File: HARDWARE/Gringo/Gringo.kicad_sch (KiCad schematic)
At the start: 7 parts, among them J1 Conn_01x06, J3 Conn_01x06, J4 Alim, J5 Conn_01x06, J6 Conn_01x06, J7 Conn_01x06, U2 BQ500212ARGZT

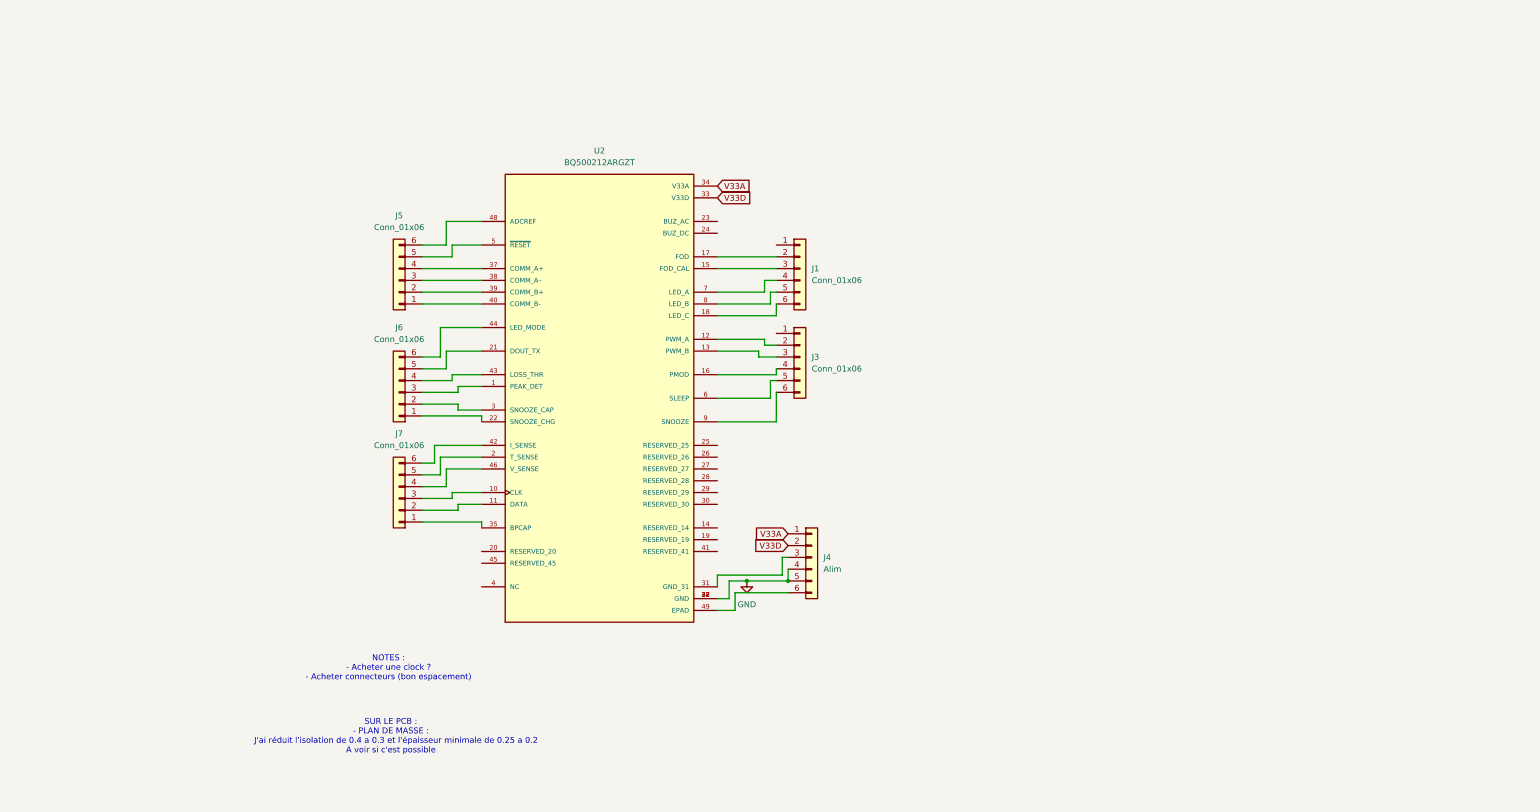
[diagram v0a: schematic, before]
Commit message: PCB test Marius - 3 composants faits
Potentiellement rajouter certains composants avant de le commander (je vais laisser faire MARIUS)
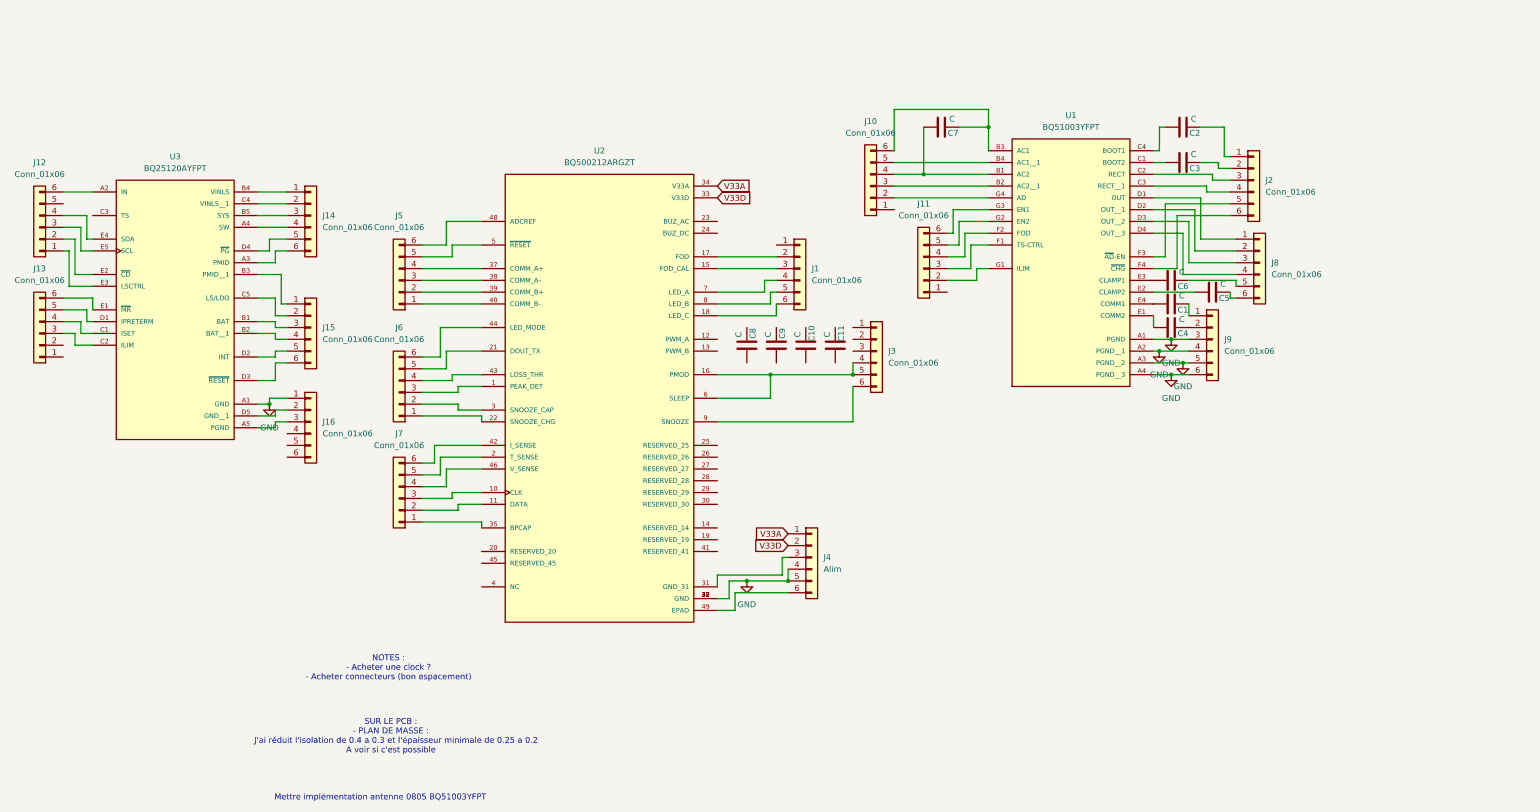
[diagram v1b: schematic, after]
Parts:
- added C1, C10, C11, C2, C3, C4, C5, C6, C7, C8, C9: C, Capacitor_SMD:C_0805_2012Metric, symbol Device:C
- added J10, J11, J12, J13, J14, J15, J16, J2, J8, J9: Conn_01x06, Connector_PinHeader_2.54mm:PinHeader_1x06_P2.54mm_Vertical, symbol Connector_Generic:Conn_01x06
- added U1: BQ51003YFPT, BQ51003YFPT:BGA28N40P7X4_300X188X50N, symbol BQ51003YFPT:BQ51003YFPT
- added U3: BQ25120AYFPT, BQ25120AYFPT:IC_BQ25120AYFPT, symbol BQ25120AYFPT:BQ25120AYFPT
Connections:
- net GND: now also J16.1 (Pin_1), J9.3 (Pin_3), J9.4 (Pin_4), J9.5 (Pin_5), J9.6 (Pin_6), U1.A1 (PGND), U1.A2 (PGND__1), U1.A3 (PGND__2), U1.A4 (PGND__3), U3.A1 (GND)
- net at U2.12 (PWM_A): no longer J3.2 (Pin_2)
- net at U2.13 (PWM_B): no longer J3.3 (Pin_3)
- net at J3.4 (Pin_4), U2.16 (PMOD): now also J3.5 (Pin_5), U2.6 (SLEEP)
- new net: C1.1, U1.E4 (COMM1)
- new net: C1.2, J9.1 (Pin_1)
- new net: J13.3 (Pin_3), U3.C2 (ILIM)
- new net: J13.4 (Pin_4), U3.C1 (ISET)
- new net: J13.5 (Pin_5), U3.D1 (IPRETERM)
- new net: J13.6 (Pin_6), U3.E1 (~{MR})
- new net: J8.1 (Pin_1), U1.D1 (OUT)
- new net: J8.2 (Pin_2), U1.D2 (OUT__1)
- new net: J8.3 (Pin_3), U1.D3 (OUT__2)
- new net: J8.4 (Pin_4), U1.D4 (OUT__3)
- new net: C6.2, J8.5 (Pin_5)
- new net: C5.2, J8.6 (Pin_6)
- new net: C3.1, U1.C1 (BOOT2)
- new net: C3.2, J2.2 (Pin_2)
- new net: C7.1, J10.4 (Pin_4), U1.B1 (AC2)
- new net: C7.2, J10.6 (Pin_6), U1.B3 (AC1)
- new net: J16.2 (Pin_2), U3.D5 (GND__1)
- new net: J16.3 (Pin_3), U3.A5 (PGND)
- new net: J10.3 (Pin_3), U1.B2 (AC2__1)
- new net: J10.5 (Pin_5), U1.B4 (AC1__1)
- new net: J2.3 (Pin_3), U1.C2 (RECT)
- new net: J2.4 (Pin_4), U1.C3 (RECT__1)
- new net: C2.1, U1.C4 (BOOT1)
- new net: C4.1, U1.E1 (COMM2)
- new net: C5.1, U1.E2 (CLAMP2)
- new net: C6.1, U1.E3 (CLAMP1)
- new net: J11.3 (Pin_3), U1.F1 (TS-CTRL)
- new net: J11.4 (Pin_4), U1.F2 (FOD)
- new net: J2.5 (Pin_5), U1.F3 (~{AD}-EN)
- new net: J2.6 (Pin_6), U1.F4 (~{CHG})
- new net: J11.2 (Pin_2), U1.G1 (ILIM)
- new net: J11.5 (Pin_5), U1.G2 (EN2)
- new net: J11.6 (Pin_6), U1.G3 (EN1)
- new net: J10.2 (Pin_2), U1.G4 (AD)
- new net: J15.1 (Pin_1), U3.B3 (PMID__1)
- new net: J15.2 (Pin_2), U3.C5 (LS/LDO)
- new net: J15.3 (Pin_3), U3.B1 (BAT)
- new net: J15.4 (Pin_4), U3.B2 (BAT__1)
- new net: J15.5 (Pin_5), U3.D2 (INT)
- new net: J15.6 (Pin_6), U3.D3 (~{RESET})
- new net: C4.2, J9.2 (Pin_2)
- new net: C2.2, J2.1 (Pin_1)
- new net: J12.1 (Pin_1), U3.E3 (LSCTRL)
- new net: J12.2 (Pin_2), U3.E2 (~{CD})
- new net: J12.3 (Pin_3), U3.E5 (SCL)
- new net: J12.4 (Pin_4), U3.E4 (SDA)
- new net: J12.6 (Pin_6), U3.A2 (IN)
- new net: J14.1 (Pin_1), U3.B4 (VINLS)
- new net: J14.2 (Pin_2), U3.C4 (VINLS__1)
- new net: J14.3 (Pin_3), U3.B5 (SYS)
- new net: J14.4 (Pin_4), U3.A4 (SW)
- new net: J14.5 (Pin_5), U3.D4 (~{PG})
- new net: J14.6 (Pin_6), U3.A3 (PMID)
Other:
- note added: "Mettre implémentation antenne 0805 BQ51003YFPT"
- moved on the sheet: J3

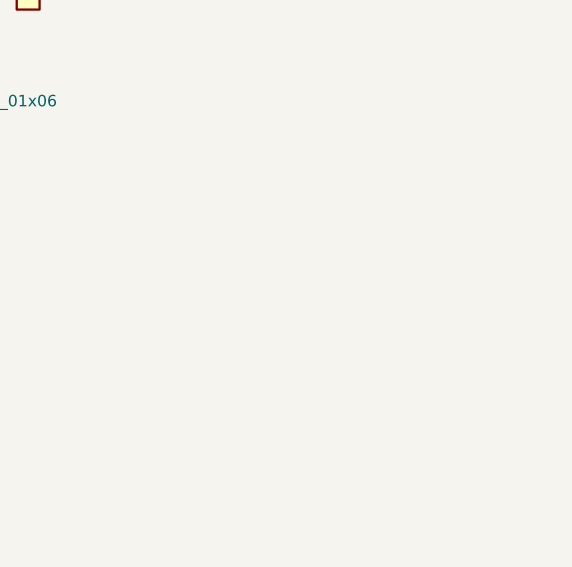
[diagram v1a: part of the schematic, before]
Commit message: Update the eval kit PCB with BPM module part
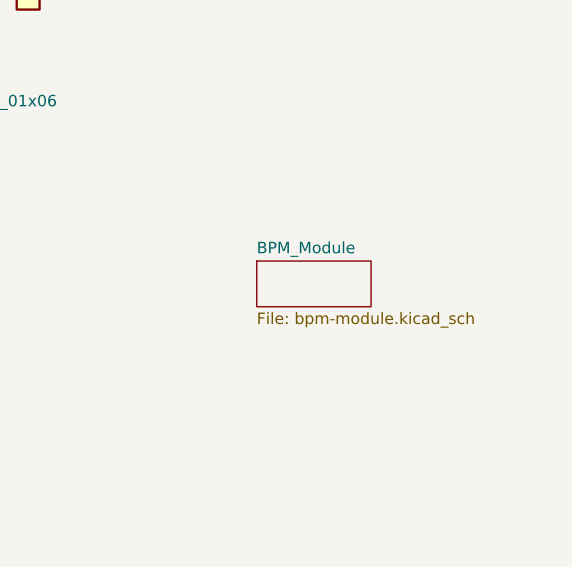
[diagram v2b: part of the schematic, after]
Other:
- added sheet BPM_Module (bpm-module.kicad_sch)
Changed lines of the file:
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@@
+		)
+	)
+	(sheet
+		(at 304.8 110.49)
+		(size 12.7 5.08)
+		(exclude_from_sim no)
+		(in_bom yes)
+		(on_board yes)
+		(dnp no)
+		(fields_autoplaced yes)
+		(stroke
+			(width 0.1524)
+			(type solid)
+		)
+		(fill
+			(color 0 0 0 0.0000)
+		)
+		(property "Sheetname" "BPM_Module"
+			(at 304.8 109.7784 0)
+			(effects
+				(font
+					(size 1.27 1.27)
+				)
+				(justify left bottom)
+			)
+		)
+		(property "Sheetfile" "bpm-module.kicad_sch"
+			(at 304.8 116.1546 0)
+			(effects
+				(font
+					(size 1.27 1.27)
+				)
+				(justify left top)
+			)
+		)
+		(instances
+			(project "Gringo"
+				(path "/d29665dc-a603-413d-b9b9-433aa1d50e1d"
+					(page "2")
+				)
+			)
 		)
 	)

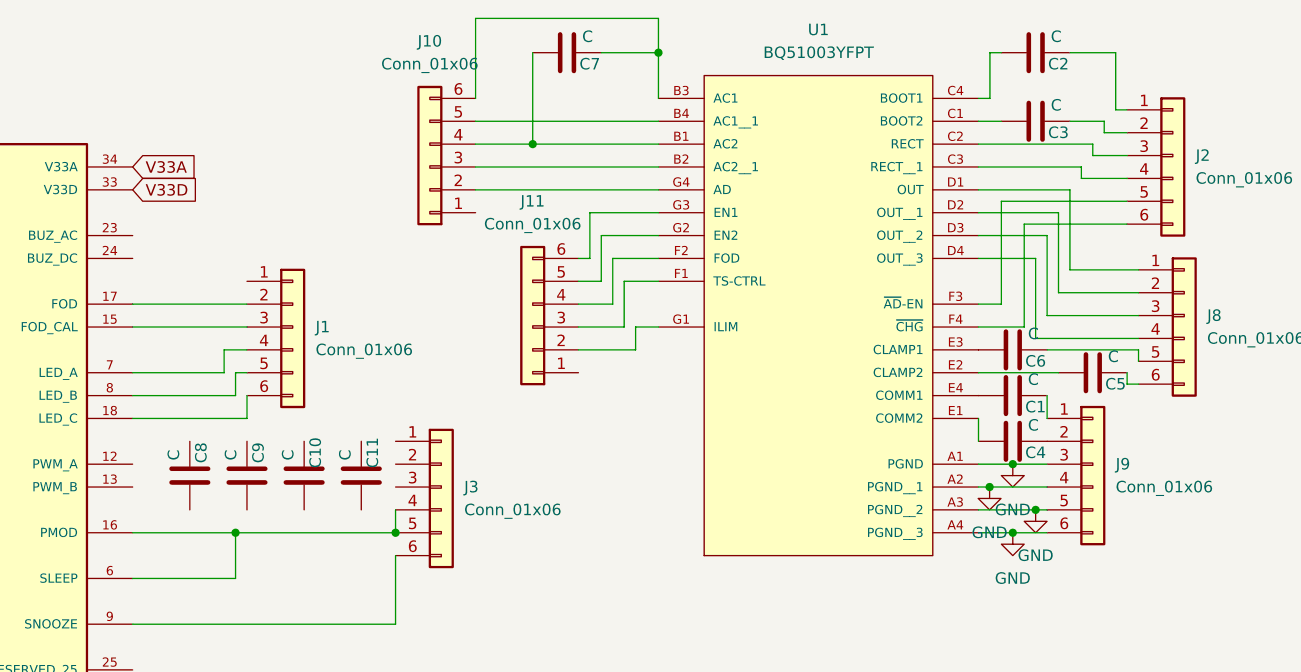
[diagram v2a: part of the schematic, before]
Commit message: Update the eval kit PCB and production files
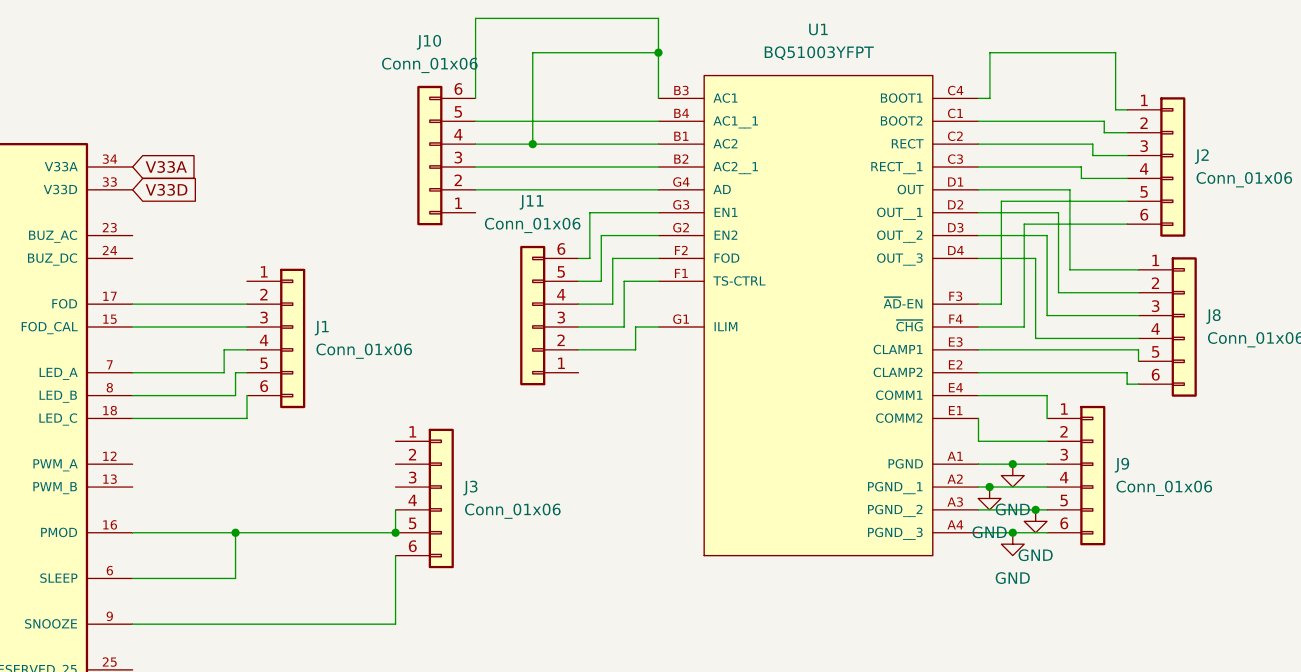
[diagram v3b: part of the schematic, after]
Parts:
- removed C1, C10, C11, C2, C3, C4, C5, C6, C7, C8, C9: C, Capacitor_SMD:C_0805_2012Metric, symbol Device:C
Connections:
- net at U1.E4 (COMM1): now also J9.1 (Pin_1)
- net at J8.5 (Pin_5): now also U1.E3 (CLAMP1)
- net at J8.6 (Pin_6): now also U1.E2 (CLAMP2)
- net at U1.C1 (BOOT2): now also J2.2 (Pin_2)
- net at J10.4 (Pin_4), U1.B1 (AC2): now also J10.6 (Pin_6), U1.B3 (AC1)
- net at U1.C4 (BOOT1): now also J2.1 (Pin_1)
- net at U1.E1 (COMM2): now also J9.2 (Pin_2)

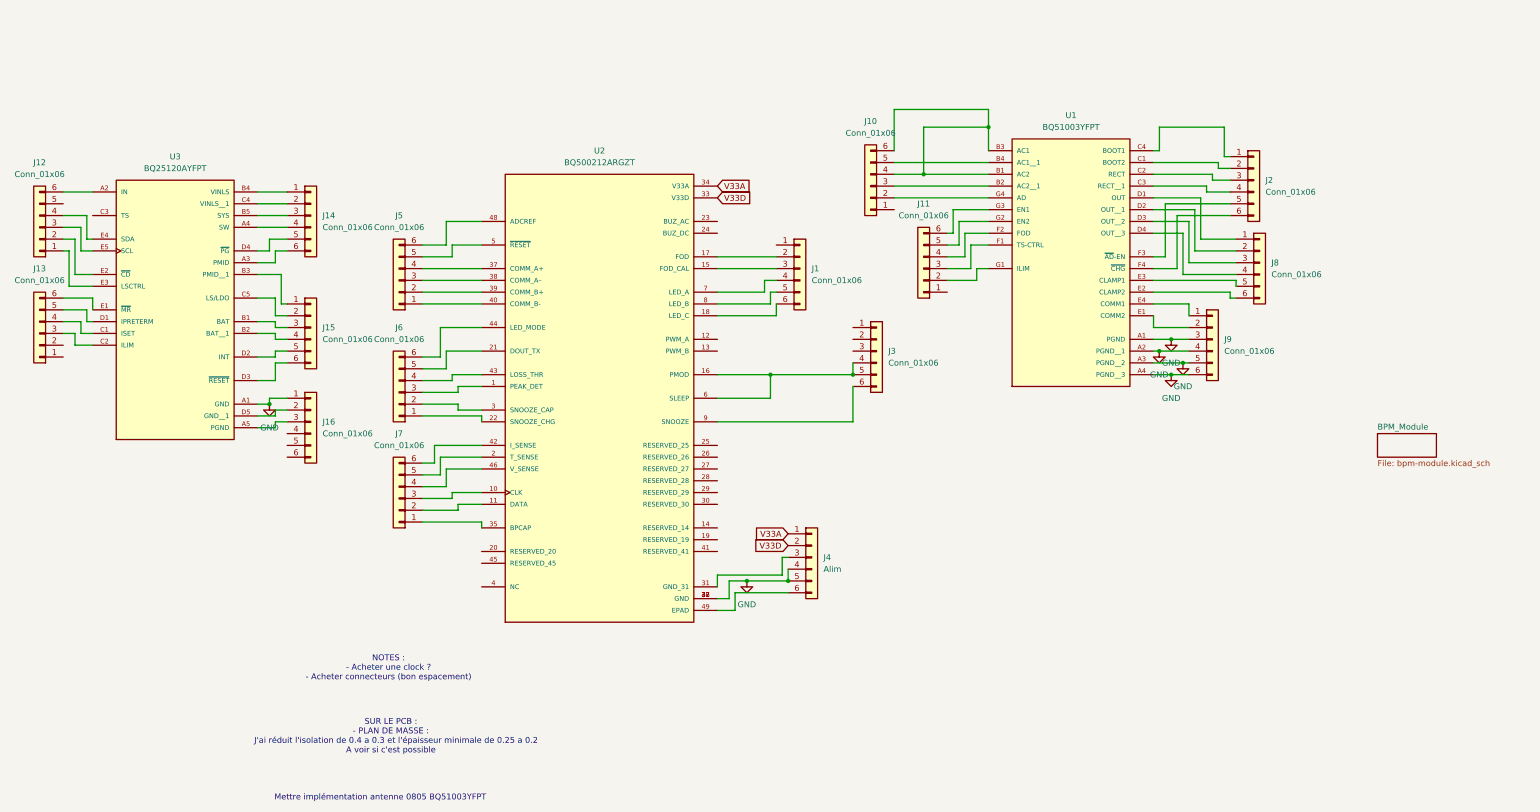
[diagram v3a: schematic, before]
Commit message: Update scheme and PCB for evk boards with adapted component packages
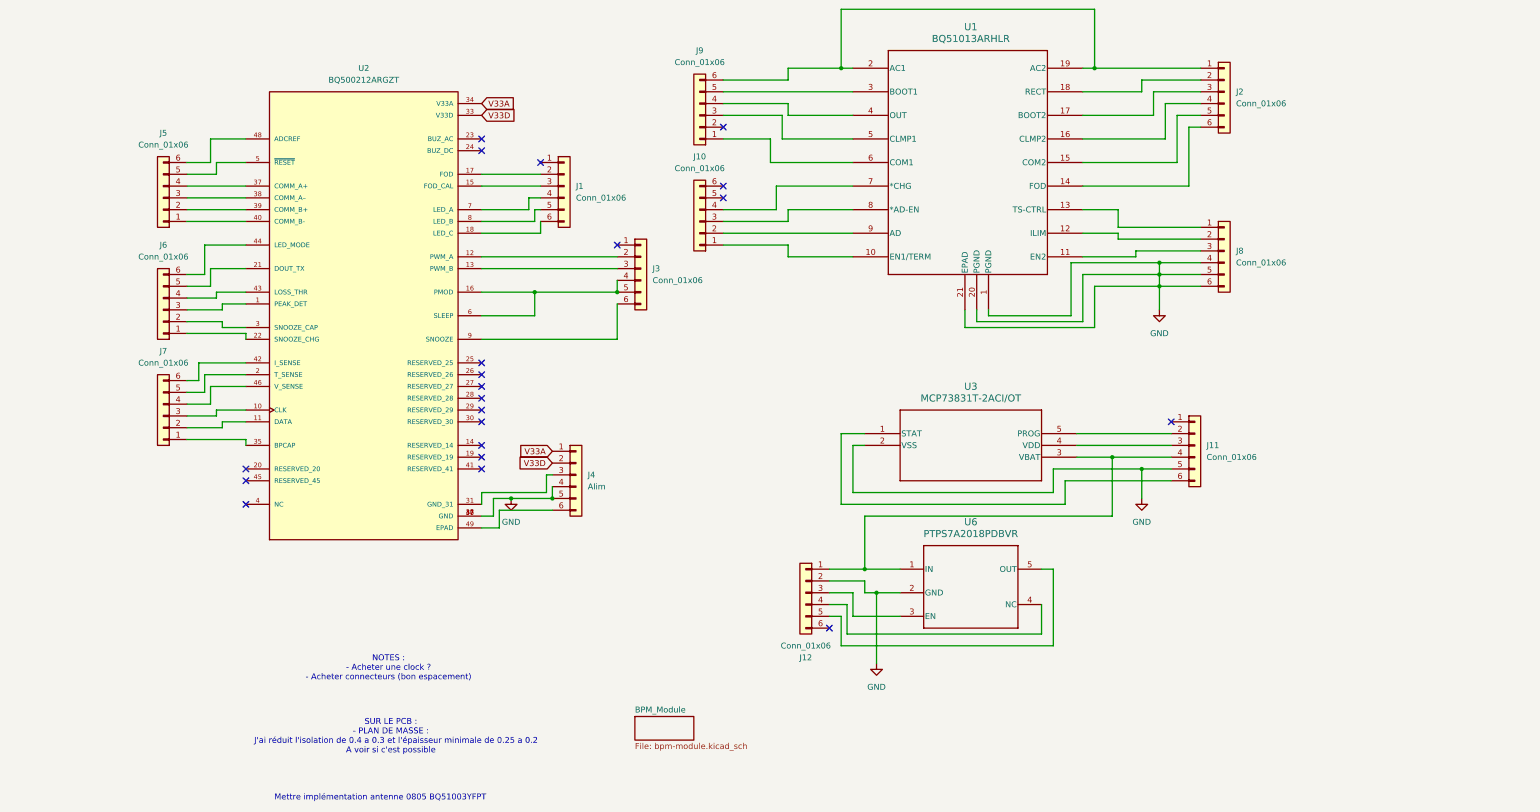
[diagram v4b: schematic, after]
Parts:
- removed J12, J14, J15, J8: Conn_01x06, Connector_PinHeader_2.54mm:PinHeader_1x06_P2.54mm_Vertical, symbol Connector_Generic:Conn_01x06
- removed U1: BQ51003YFPT, BQ51003YFPT:BGA28N40P7X4_300X188X50N, symbol BQ51003YFPT:BQ51003YFPT
- removed U3: BQ25120AYFPT, BQ25120AYFPT:IC_BQ25120AYFPT, symbol BQ25120AYFPT:BQ25120AYFPT
- added U1: BQ51013ARHLR, RHL20_2P05X3P05, symbol BQ51013ARHLR:BQ51013ARHLR
- added U3: MCP73831T-2ACI/OT, SOT-23-5_MC_MCH, symbol MCP73831T-2ACI-OT:MCP73831T-2ACI_OT
- added U6: PTPS7A2018PDBVR, DBV0005A-IPC_A, symbol PTPS7A2018PDBVR:PTPS7A2018PDBVR
- U2: footprint tonpere:IC_BQ500212ARGZT -> BQ500212ARGZT:RGZ0048A
- renumbered J11 to J10, J16 to J11, J13 to J12, J9 to J8, J10 to J9
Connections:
- net GND: now also J11.5 (Pin_5), J12.2 (Pin_2), U1.1 (PGND), U1.20 (PGND), U1.21 (EPAD), U3.2 (VSS), U6.2 (GND); no longer J11.1 (Pin_1), J8.3 (Pin_3)
- net at J12.1 (Pin_1): now also J11.4 (Pin_4), U3.3 (VBAT), U6.1 (IN)
- net at J12.3 (Pin_3): now also U6.3 (EN)
- net at J12.4 (Pin_4): now also U6.4 (NC)
- net at J12.5 (Pin_5): now also U6.5 (OUT)
- net at J11.2 (Pin_2): now also U3.5 (PROG)
- net at J11.3 (Pin_3): now also U3.4 (VDD)
- net at J11.6 (Pin_6): now also U3.1 (STAT)
- net at J9.6 (Pin_6): now also J2.1 (Pin_1), U1.19 (AC2), U1.2 (AC1); no longer J9.4 (Pin_4)
- net at J9.3 (Pin_3): now also U1.5 (CLMP1)
- net at J9.5 (Pin_5): now also U1.3 (BOOT1)
- net at J2.2 (Pin_2): now also U1.18 (RECT)
- net at J2.3 (Pin_3): now also U1.17 (BOOT2)
- net at J2.4 (Pin_4): now also U1.16 (CLMP2)
- net at J8.2 (Pin_2): now also U1.12 (ILIM)
- net at J8.1 (Pin_1): now also U1.13 (TS-CTRL)
- net at J10.3 (Pin_3): now also U1.8 (*AD-EN)
- net at J10.4 (Pin_4): now also U1.7 (*CHG)
- net at J2.5 (Pin_5): now also U1.15 (COM2)
- net at J2.6 (Pin_6): now also U1.14 (FOD)
- net at J10.2 (Pin_2): now also U1.9 (AD)
- net at U2.12 (PWM_A): now also J3.2 (Pin_2)
- net at U2.13 (PWM_B): now also J3.3 (Pin_3)
- net at J10.1 (Pin_1): now also U1.10 (EN1/TERM)
- net at J9.1 (Pin_1): now also U1.6 (COM1)
- new net: J8.3 (Pin_3), U1.11 (EN2)
- new net: J9.4 (Pin_4), U1.4 (OUT)
- no-connect marks 0 -> 21
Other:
- moved on the sheet: J1, J10, J11, J12, J2, J3, J4, J5, J6, J7, J8, J9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
